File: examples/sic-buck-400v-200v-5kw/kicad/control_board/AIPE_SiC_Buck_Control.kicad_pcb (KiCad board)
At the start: 4 copper layers, 120 x 80 mm, 207 parts, among them J1 12 V in, J2 J_RESET: manual reset through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, J3 J_JTAG: TI 14-pin, key pin 6 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, J4 J_BOOT: jumper 1-2 = SCI-A bo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, J5 J_UART: SCI-A, 3.3 V levels o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, J6 J_ESTOP: normally-closed E-st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, J7 J_NTC: Vishay NTCALUG01A103F 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, J8 J_MEZZ: 2 x 25 header to the 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, Q1 MMBT3904,215, U1 TPS26400PWPR, U10 SN74LV21APWR, U11 SN74LV04APWR, U12 REF3125AIDBZR, U13 TLV1702AIDGKR, U14 TLV1702AIDGKR, U15 REF3130AIDBZR, U16 LM61CIM3/NOPB, U2 TPS54302DDCR, U3 TPS767D301PWPR, U4 TPS3808G01DBVR, U5 TMS320F28335PGFA, U6 SN74LVC2G08DCTR, U7 SN74LVC1G74DCTR, U8 SN74LV21APWR, U9 SN74LV21APWR, Y1 ASV-30.000MHZ-EJ-T

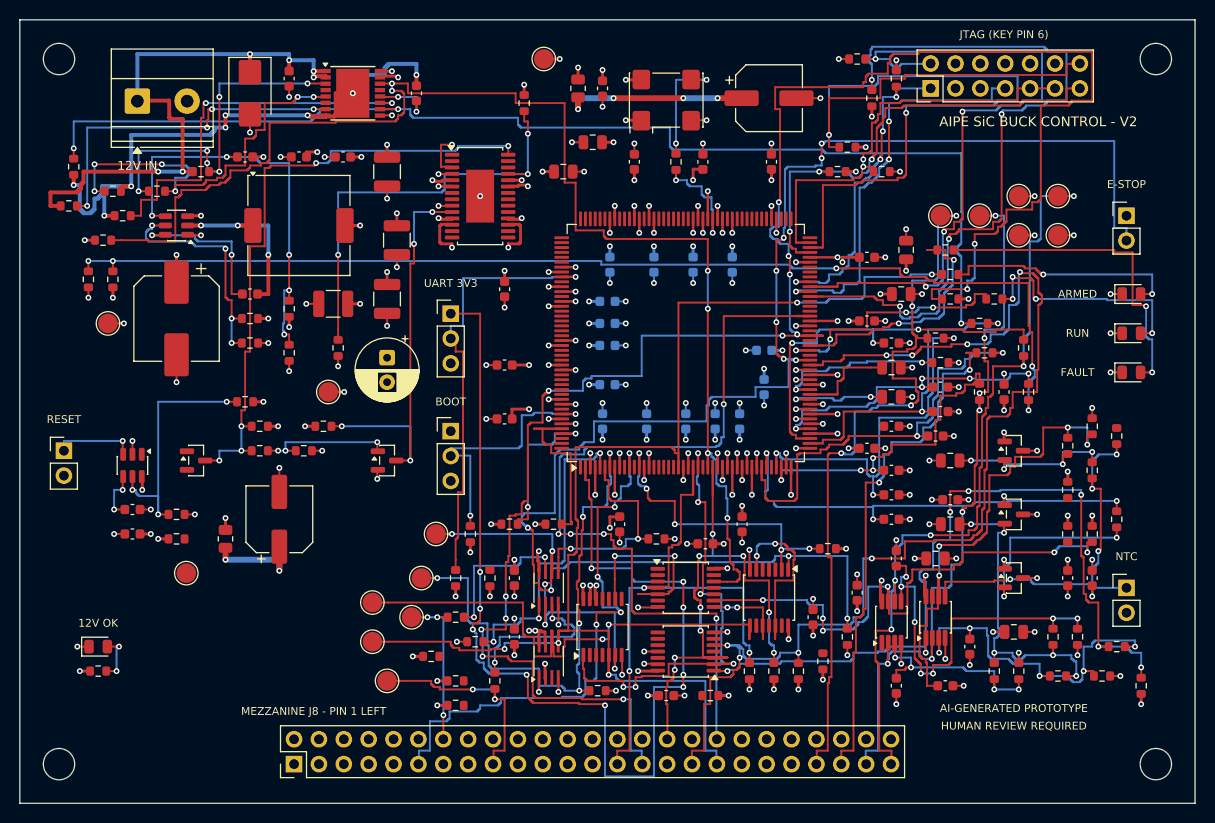
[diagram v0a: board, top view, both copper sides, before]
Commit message: feat(pcb): both V2 boards placed, routed and at native DRC zero; exports, metrics, review and correction pass
Power board AIPE_SiC_Buck_Power (240 x 180 mm, 4 x 70 um): 237 footprints, 4755 tracks,
606 vias, 36 zones, router 0 open; kicad-cli DRC --schematic-parity --severity-all
0 violations / 0 unconnected / 0 parity (verification/drc/20261011T054445Z-drc-d0914d79,
board sha256 b1bb5698...). Stored zone fills are the rule-aware copper (no-refill DRC
499 -> 0, engineering_checks/stored_zone_fill_check_power.json).

Control board AIPE_SiC_Buck_Control (120 x 80 mm, 4 x 35 um): 207 footprints, 5995 tracks,
798 vias, 20 zones, router 0 open; DRC 0 / 0 / 0 (20261011T051246Z-drc-f801ed3c, sha256
dead06ed...).

Live generators generate_sic_power_board.py / generate_sic_control_board.py (placement
from design/placement_*.json, grid router plans, corridor zones, rule-aware refill,
metrics, DRC), grid_router.py lane memory / two-pass retry / rip-up negotiation, every
DRC manifest of the convergence (51 runs), routing_progress / routing_iterations,
layout metrics, netlist checks (exact match), eleven exports per board with hashed
manifests, renders and layer PDFs, independent layout review (pcb_rule_review.md,
layout_review_findings.json LR-20..LR-35), correction pass before/after
(optimisation_before_after.*, pass 2 report script), V1/V2 comparison refresh.
verify_sic_buck passes; 253 unit tests pass (floorplan candidate B amended for the
slotted UCC21710 footprint). No DRC rule weakened; unresolved review items LR-22,
LR-24, LR-26, LR-27, LR-32, LR-33 documented for human review.

Co-Authored-By: Claude Fable 5.1 <noreply@anthropic.com>
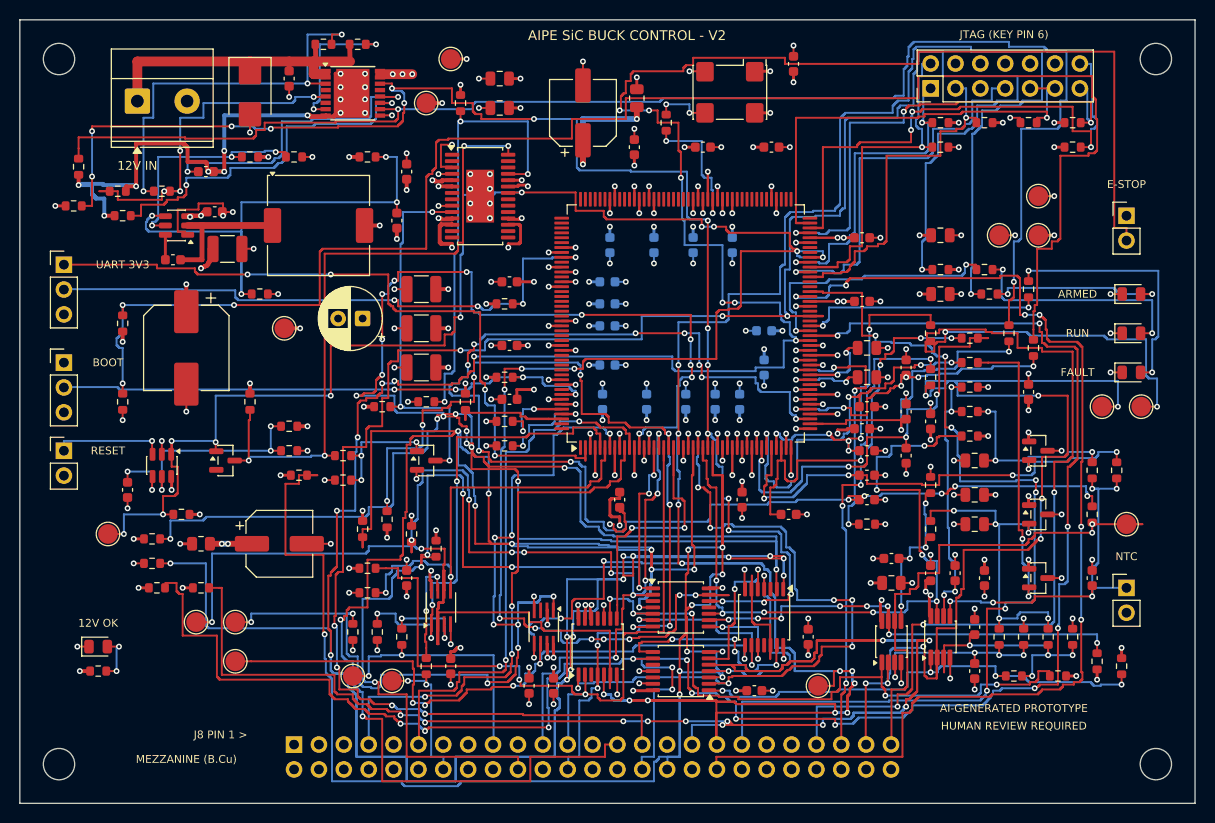
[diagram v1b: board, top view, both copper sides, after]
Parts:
- J8: moved to B.Cu
- moved R52 71.4 mm to (13.5, 55.5), turned to 180 degrees
- moved R51 69.0 mm to (13.5, 53.0), turned to 0 degrees
- moved R50 68.4 mm to (14.0, 58.0), turned to 0 degrees
- moved C55 63.1 mm to (44.0, 66.0), turned to -90 degrees
- moved R49 61.6 mm to (18.5, 58.0), turned to 0 degrees
- moved R48 52.5 mm to (28.5, 46.5), turned to 0 degrees
- moved TP9 45.7 mm to (81.5, 68.0)
- moved R47 42.1 mm to (35.0, 52.0), turned to -90 degrees
- moved J4 40.1 mm to (4.50, 35.0)
- moved J5 39.8 mm to (4.50, 25.0)
- moved TP4 39.5 mm to (41.5, 8.50)
- moved R46 37.6 mm to (37.5, 51.0), turned to 90 degrees
- moved TP15 34.2 mm to (113.0, 51.5)
- moved R6 33.8 mm to (34.5, 2.50)
- moved R41 30.0 mm to (35.5, 58.5), turned to 180 degrees
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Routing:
- net ESTOP_N: track 168.8 -> 402.5 mm, vias 11 -> 24
- net XRS_N: track 0.28 -> 226.1 mm, vias 0 -> 21
- net PG_BIAS_S_N: track 0.10 -> 213.2 mm, vias 0 -> 15
- net DSP_TRIP_N: track 32.2 -> 224.4 mm, vias 5 -> 21
- net FAULT_N: track 133.8 -> 319.7 mm, vias 5 -> 16
- net OC_N: track 57.9 -> 204.1 mm, vias 3 -> 10
- net FLT_H_N: track 0.10 -> 105.4 mm, vias 0 -> 8
- net PG_BIAS_L_N: track 126.9 -> 228.5 mm, vias 8 -> 12
- net SPARE_D2: track 0.00 -> 99.6 mm, vias 0 -> 7
- net RDY_L: track 0.06 -> 99.2 mm, vias 0 -> 9
- net ADC_VOUT: track 42.5 -> 139.2 mm, vias 3 -> 14
- net FLT_L_N: track 0.10 -> 92.4 mm, vias 0 -> 10
- net PG_BIAS_H_N: track 73.7 -> 163.0 mm
- net RDY_H: track 0.10 -> 77.7 mm, vias 0 -> 3
- net OTP_N: track 0.13 -> 76.7 mm, vias 0 -> 8
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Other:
- board text added: "J8 PIN 1 >"
- board text added: "MEZZANINE (B.Cu)"
- board text removed: "MEZZANINE J8 - PIN 1 LEFT"

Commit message: feat(v2.1): example regenerated - wired schematics, both boards routed with the upgraded router, exports, crops, validation
Schematics (wired style, gates passed): ERC 0 on both projects (power 20261012T075113Z-erc-df18ce6e,
control 20261012T075120Z-erc-7a14cacb); netlist (ref,pad)->net exact vs the model and vs the frozen V2
netlists with equal net names; .kicad_dru / net_settings identical to the legacy generation; stub
global labels 648 -> 7 (power) and 667 -> 7 (control), wired pin share 0 -> 0.90 / 0.76, junctions,
hierarchical labels and power symbols introduced, continuation sheets removed; readability metrics
V2 vs V2.1 in engineering_checks/schematic_readability_*.

Power board (octilinear simplification + tangent arcs on the V2 search; 8-direction search kept
opt-in after attempt A left 2 connections open): 0 unresolved, DRC 0/0/0 (20261012T090308Z-drc-8fd50803),
segments 4755 -> 2991 + 145 arcs, 90-degree bends 3609 -> 1121, stair runs 382 -> 124, length
5744.6 -> 5545.6 mm, vias 606 = V2, no net longer / more vias / narrower. Control board: 0 unresolved,
DRC 0/0/0 (20261012T084327Z-drc-7f07f983), segments 5995 -> 4262 + 261 arcs, 90-degree bends
4069 -> 1233, stair runs 435 -> 144, length 7055.2 -> 6700.7 mm, vias 798 = V2, 96 nets shorter,
0 longer. FOOTPRINT.SetDNP for DNP parts (schematic parity), beautify anchors bound to off-grid vias
by copper overlap (path_geometry.connected_by_overlap), In2.Cu inner pass styled.

Exports 11/11 per board, renders and layer PDFs refreshed, high-resolution V2/V2.1 crops under
review/crops/, routing_quality_* and v21_validation.{json,md} (nine TASK 7 checks independently
re-derived). verify_sic_buck passed; 338 tests OK (2 skipped).

Co-Authored-By: Claude Fable 5.1 <noreply@anthropic.com>
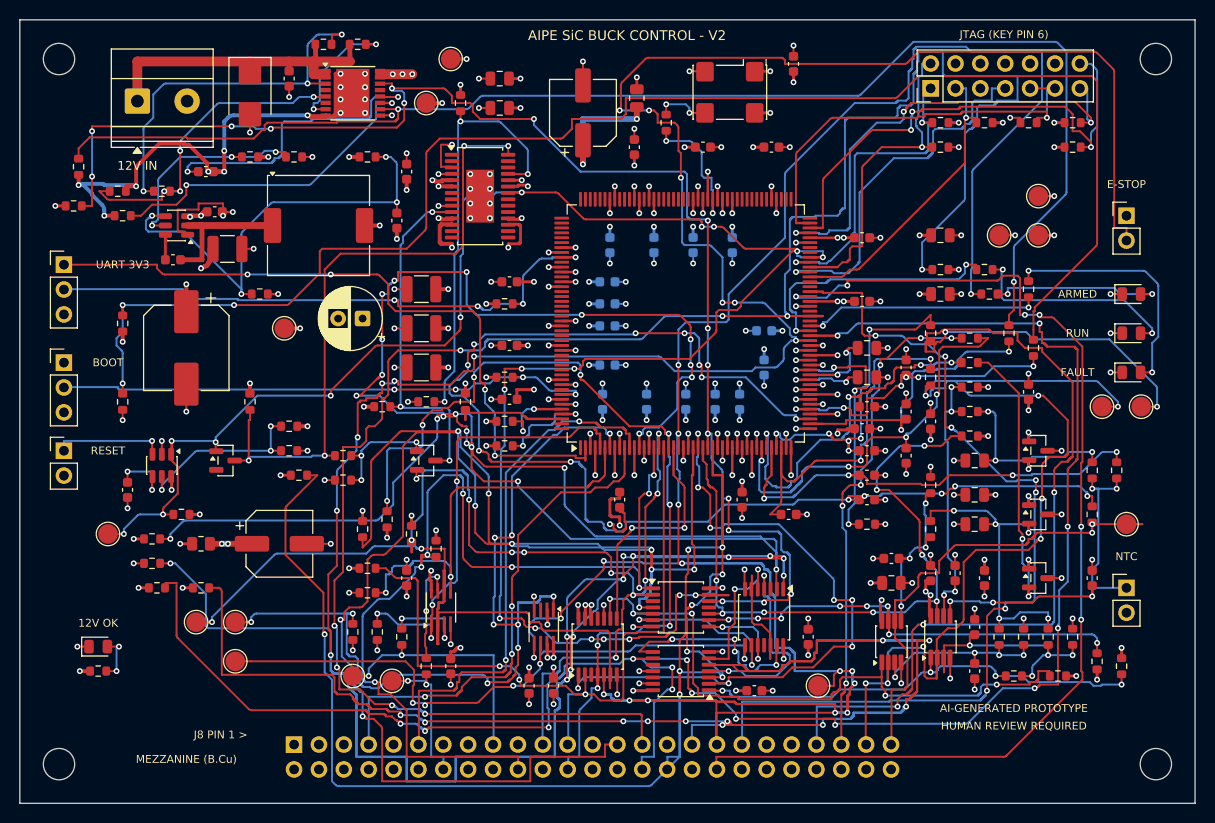
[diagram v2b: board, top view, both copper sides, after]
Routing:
- net XRS_N: track 226.1 -> 206.6 mm
- net ESTOP_N: track 402.5 -> 384.6 mm
- net DSP_TRIP_N: track 224.4 -> 207.1 mm
- net FAULT_N: track 319.7 -> 303.0 mm
- net PG_BIAS_S_N: track 213.2 -> 201.0 mm
- net V12V_MON: track 167.6 -> 156.5 mm
- net OC_N: track 204.1 -> 193.5 mm
- net PG_BIAS_H_N: track 163.0 -> 153.4 mm
- net I12V_MON: track 149.8 -> 140.2 mm
- net FAN_TACH: track 214.0 -> 205.0 mm
- net SPARE_D1: track 121.0 -> 113.3 mm
- net VIN_SENSE: track 111.5 -> 103.8 mm
- net ISENSE: track 122.2 -> 114.5 mm
- net ADC_VOUT: track 139.2 -> 131.9 mm
- net TDI: track 37.9 -> 31.0 mm
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
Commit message: chore(v2.1): one generation label (sic_buck_common.GENERATION) and a reproducible full regeneration
GENERATION = "V2.1" derives BANNER, REVISION, title-block comments, .kicad_dru headers,
NOTICE.md, the power-board silkscreen and the control-board label (kept at the V2 label
length so the placer's text obstacle box, and therefore the placement, is unchanged).
Models, schematics (ERC 0: 20261012T094955Z-erc-c574a866 / 20261012T095007Z-erc-caa10a79,
all gates passed), both boards (DRC 0/0/0: power 20261012T100423Z-drc-8b9e64d1, control
20261012T103755Z-drc-0a4fa5cf), netlist checks, routing-quality records (totals, per-layer
and per-net tables identical to the previous commit), exports (11/11 each), renders, V2.1
crops (same framing; V2 crops untouched) and readability reports regenerated. Independent
re-validation in verification/v21_validation.{json,md} (12 rows). verify_sic_buck passed;
340 tests OK (2 skipped). Known residue: control-board corridor zone priorities depend on
reload order (same zones, DRC clean), manufacturing/README.md still describes the V2 bundle.

Co-Authored-By: Claude Fable 5.1 <noreply@anthropic.com>
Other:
- board text added: "AIPE SiC BUCK CONTROL V2.1"
- board text removed: "AIPE SiC BUCK CONTROL - V2"
